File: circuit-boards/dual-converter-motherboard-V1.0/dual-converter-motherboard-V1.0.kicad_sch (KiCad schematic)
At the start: 32 parts, among them J1 2601-1102, J2 2601-1102, J3 S4B-XH-SM4-TB, U1 POWER_MANAGEMENT_MODULE, U2 HIGH-CURRENT_PHASE_MODULE_V1.0, U3 HIGH-VOLTAGE_PHASE_MODULE

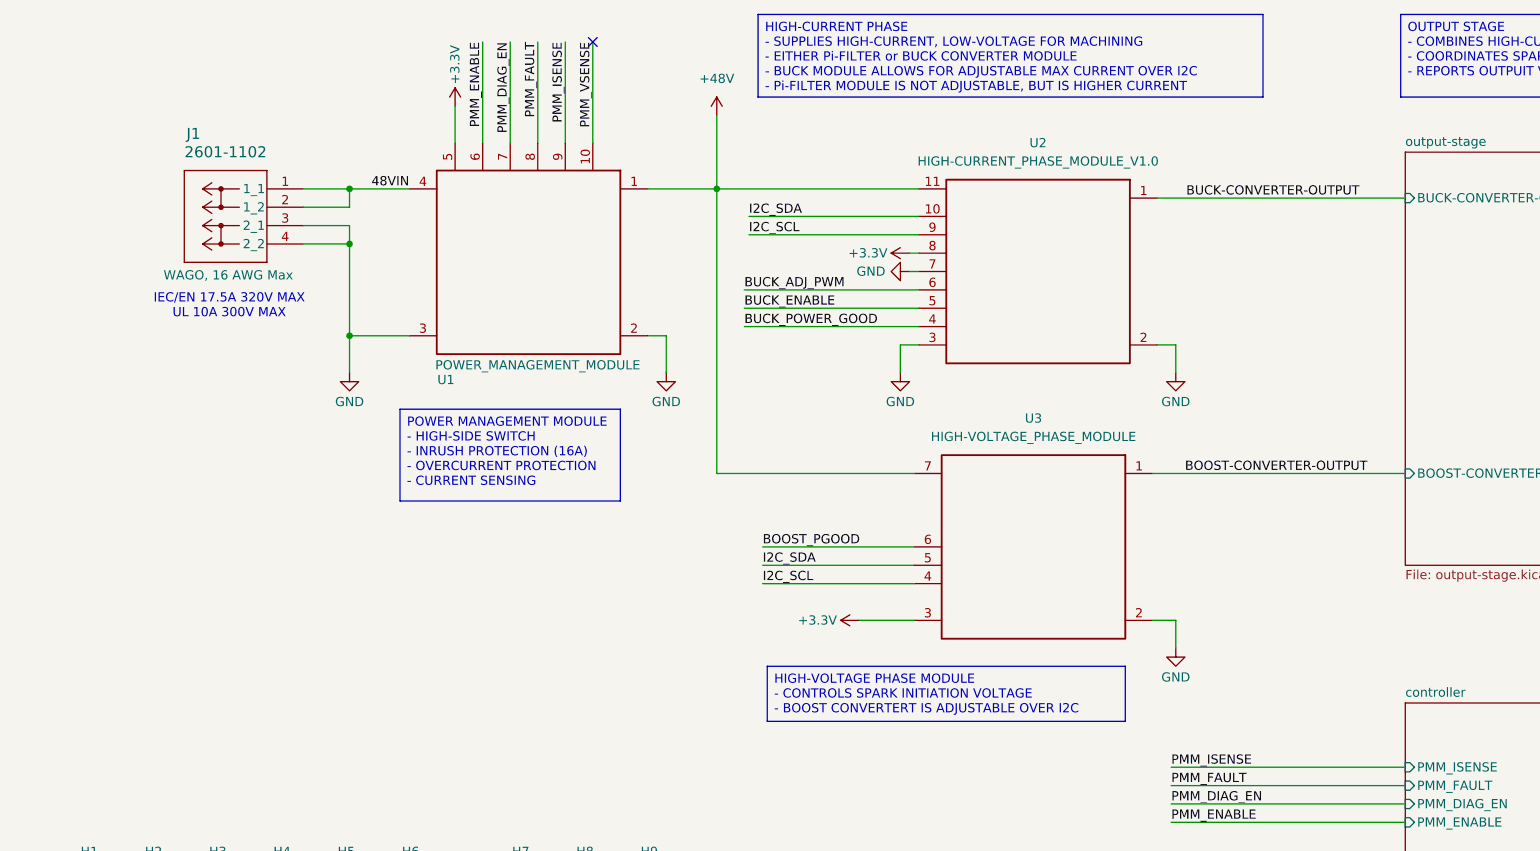
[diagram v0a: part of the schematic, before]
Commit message: begin replacing pogo pins with pin headers. todo: fix ugly schematic, add non power connections
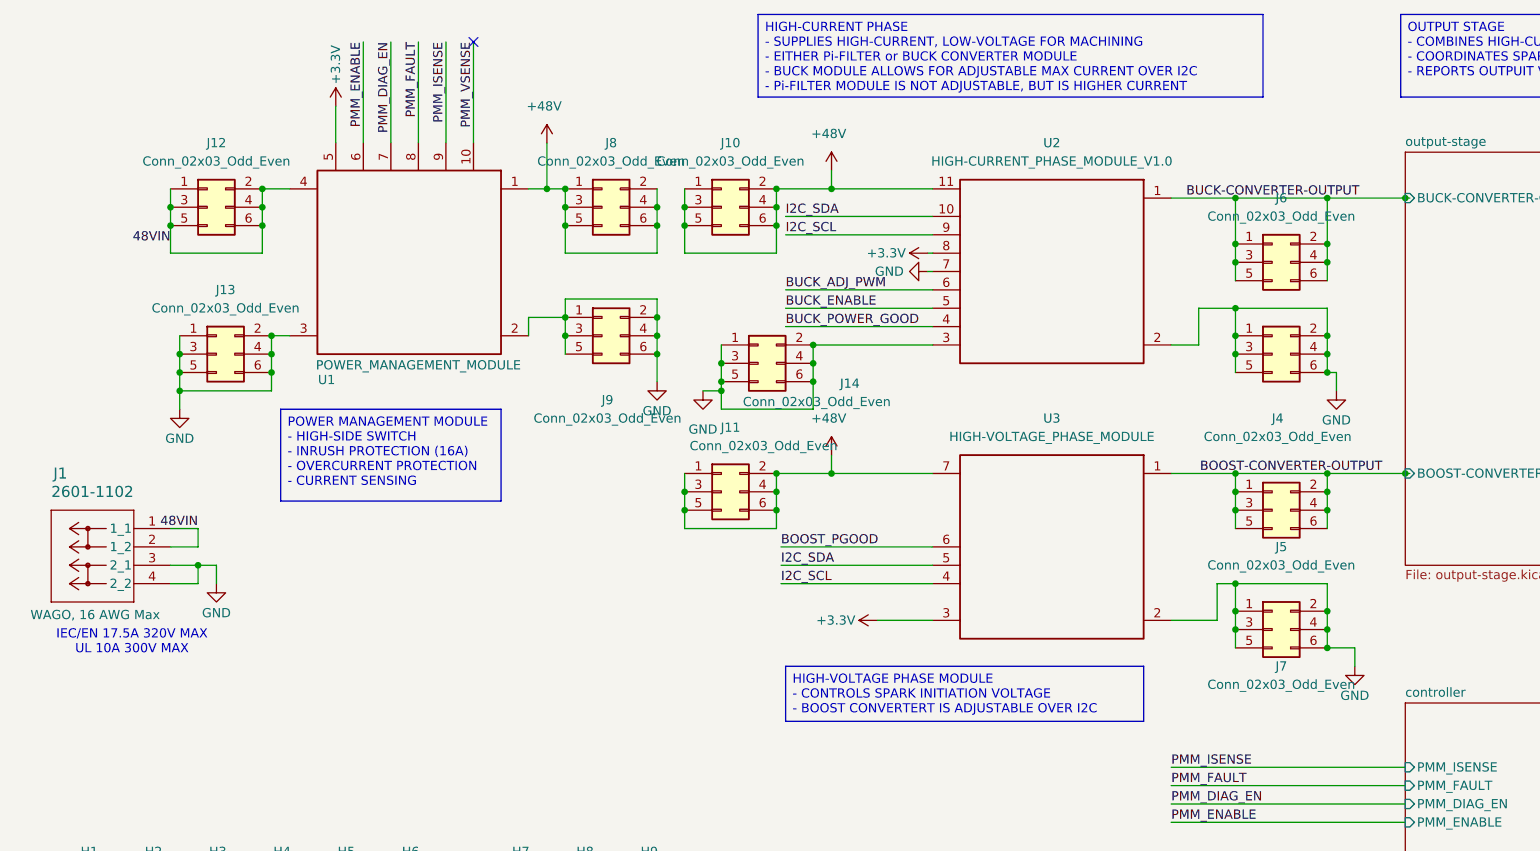
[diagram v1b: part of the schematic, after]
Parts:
- added J10, J11, J12, J13, J14, J4, J5, J6, J7, J8, J9: Conn_02x03_Odd_Even, Connector_PinSocket_2.54mm:PinSocket_2x03_P2.54mm_Vertical, symbol Connector_Generic:Conn_02x03_Odd_Even
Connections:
- net +48V: now also J10.1 (Pin_1), J10.2 (Pin_2), J10.3 (Pin_3), J10.4 (Pin_4), J10.5 (Pin_5), J10.6 (Pin_6), J11.1 (Pin_1), J11.2 (Pin_2), J11.3 (Pin_3), J11.4 (Pin_4), J11.5 (Pin_5), J11.6 (Pin_6), J8.1 (Pin_1), J8.2 (Pin_2), J8.3 (Pin_3), J8.4 (Pin_4), J8.5 (Pin_5), J8.6 (Pin_6)
- net 48VIN: now also J12.1 (Pin_1), J12.2 (Pin_2), J12.3 (Pin_3), J12.4 (Pin_4), J12.5 (Pin_5), J12.6 (Pin_6)
- net BOOST-CONVERTER-OUTPUT: now also J5.1 (Pin_1), J5.2 (Pin_2), J5.3 (Pin_3), J5.4 (Pin_4), J5.5 (Pin_5), J5.6 (Pin_6)
- net BUCK-CONVERTER-OUTPUT: now also J6.1 (Pin_1), J6.2 (Pin_2), J6.3 (Pin_3), J6.4 (Pin_4), J6.5 (Pin_5), J6.6 (Pin_6)
- net GND: now also J13.1 (Pin_1), J13.2 (Pin_2), J13.3 (Pin_3), J13.4 (Pin_4), J13.5 (Pin_5), J13.6 (Pin_6), J14.1 (Pin_1), J14.2 (Pin_2), J14.3 (Pin_3), J14.4 (Pin_4), J14.5 (Pin_5), J14.6 (Pin_6), J4.1 (Pin_1), J4.2 (Pin_2), J4.3 (Pin_3), J4.4 (Pin_4), J4.5 (Pin_5), J4.6 (Pin_6), J7.1 (Pin_1), J7.2 (Pin_2), J7.3 (Pin_3), J7.4 (Pin_4), J7.5 (Pin_5), J7.6 (Pin_6), J9.1 (Pin_1), J9.2 (Pin_2), J9.3 (Pin_3), J9.4 (Pin_4), J9.5 (Pin_5), J9.6 (Pin_6)
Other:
- moved on the sheet: J1, U1, U2, U3
